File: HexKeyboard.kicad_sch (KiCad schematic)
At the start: 62 parts, among them J1 Conn_02x04_Odd_Even, J4 USB_A, J9 Micro_SD_Card, SW1 SW_3, SW10 SW_9, SW11 SW_8, SW12 SW_7, SW13 SW_Hash, SW14 SW_Hash, SW15 SW_0, SW16 SW_Star, SW17 SW_Hash, SW18 SW_Hash, SW19 SW_0, SW2 SW_3, SW20 SW_Star, SW3 SW_2, SW4 SW_1, SW5 SW_6, SW6 SW_6, SW7 SW_5, SW8 SW_4, SW9 SW_9, U1 ATmega32U4-AU, U2 AMS1117-3.3, U3 74LVC125, U4 AT24CS64-XHM, Y1 16MHz

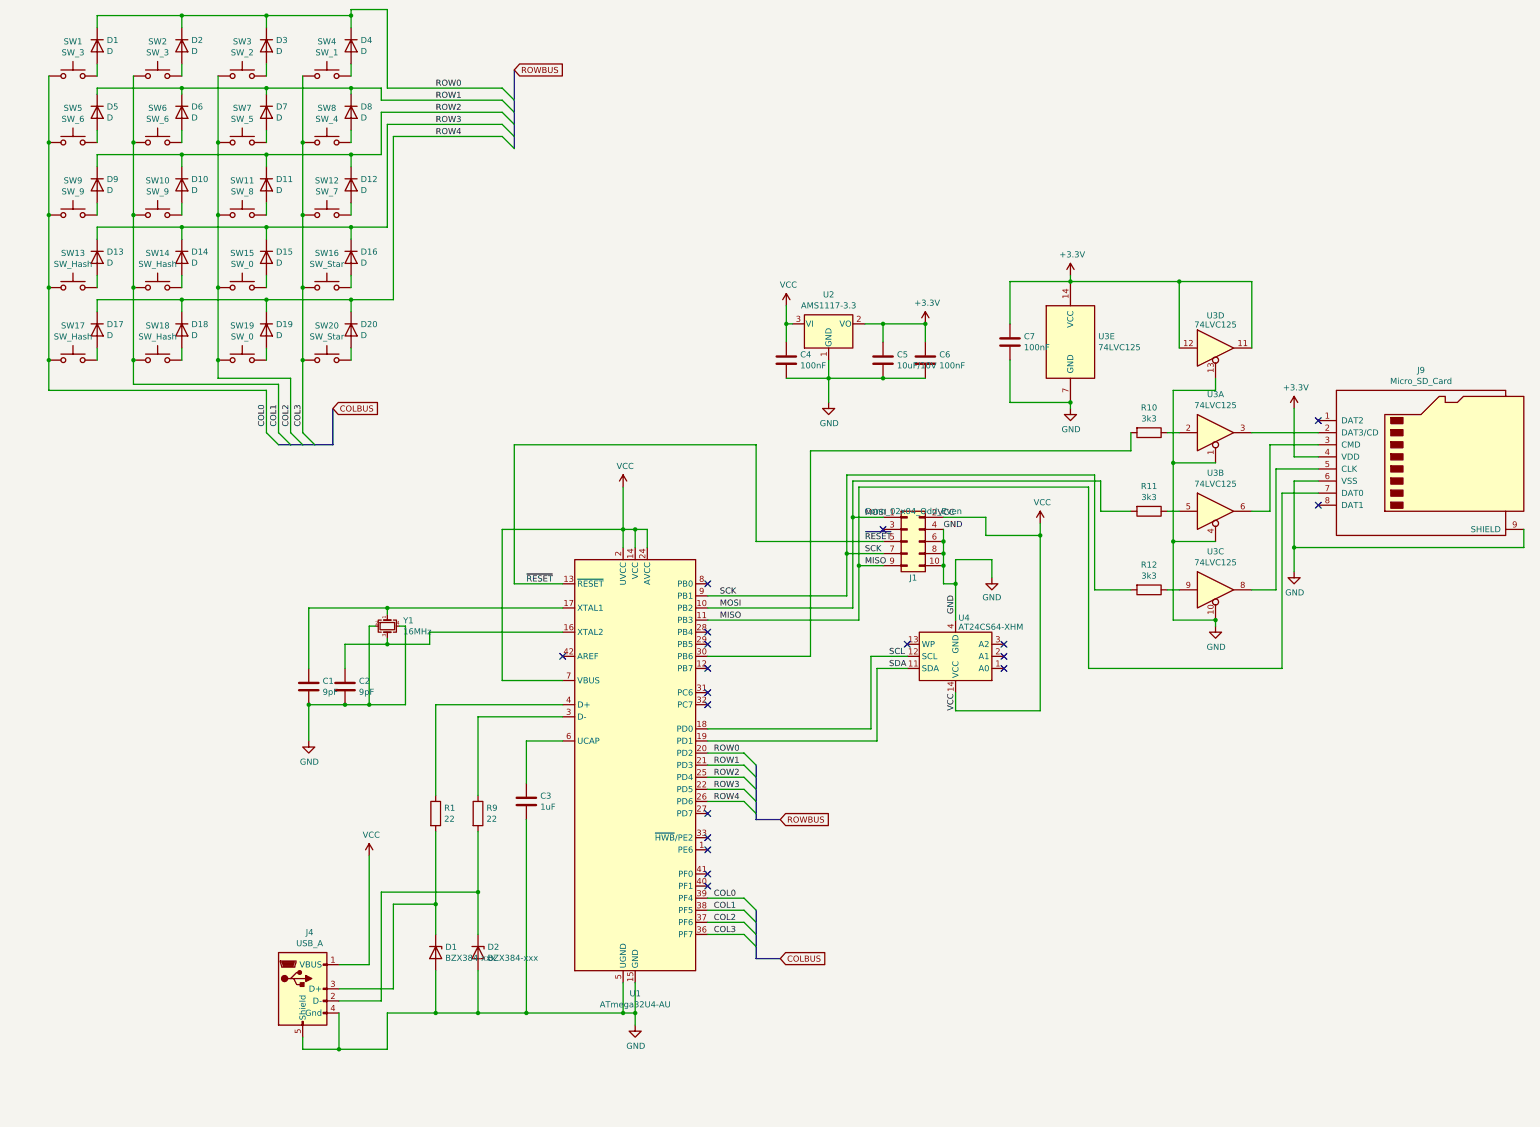
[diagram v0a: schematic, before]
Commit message: Cleaned up libraries Added Display Switched to USB-C
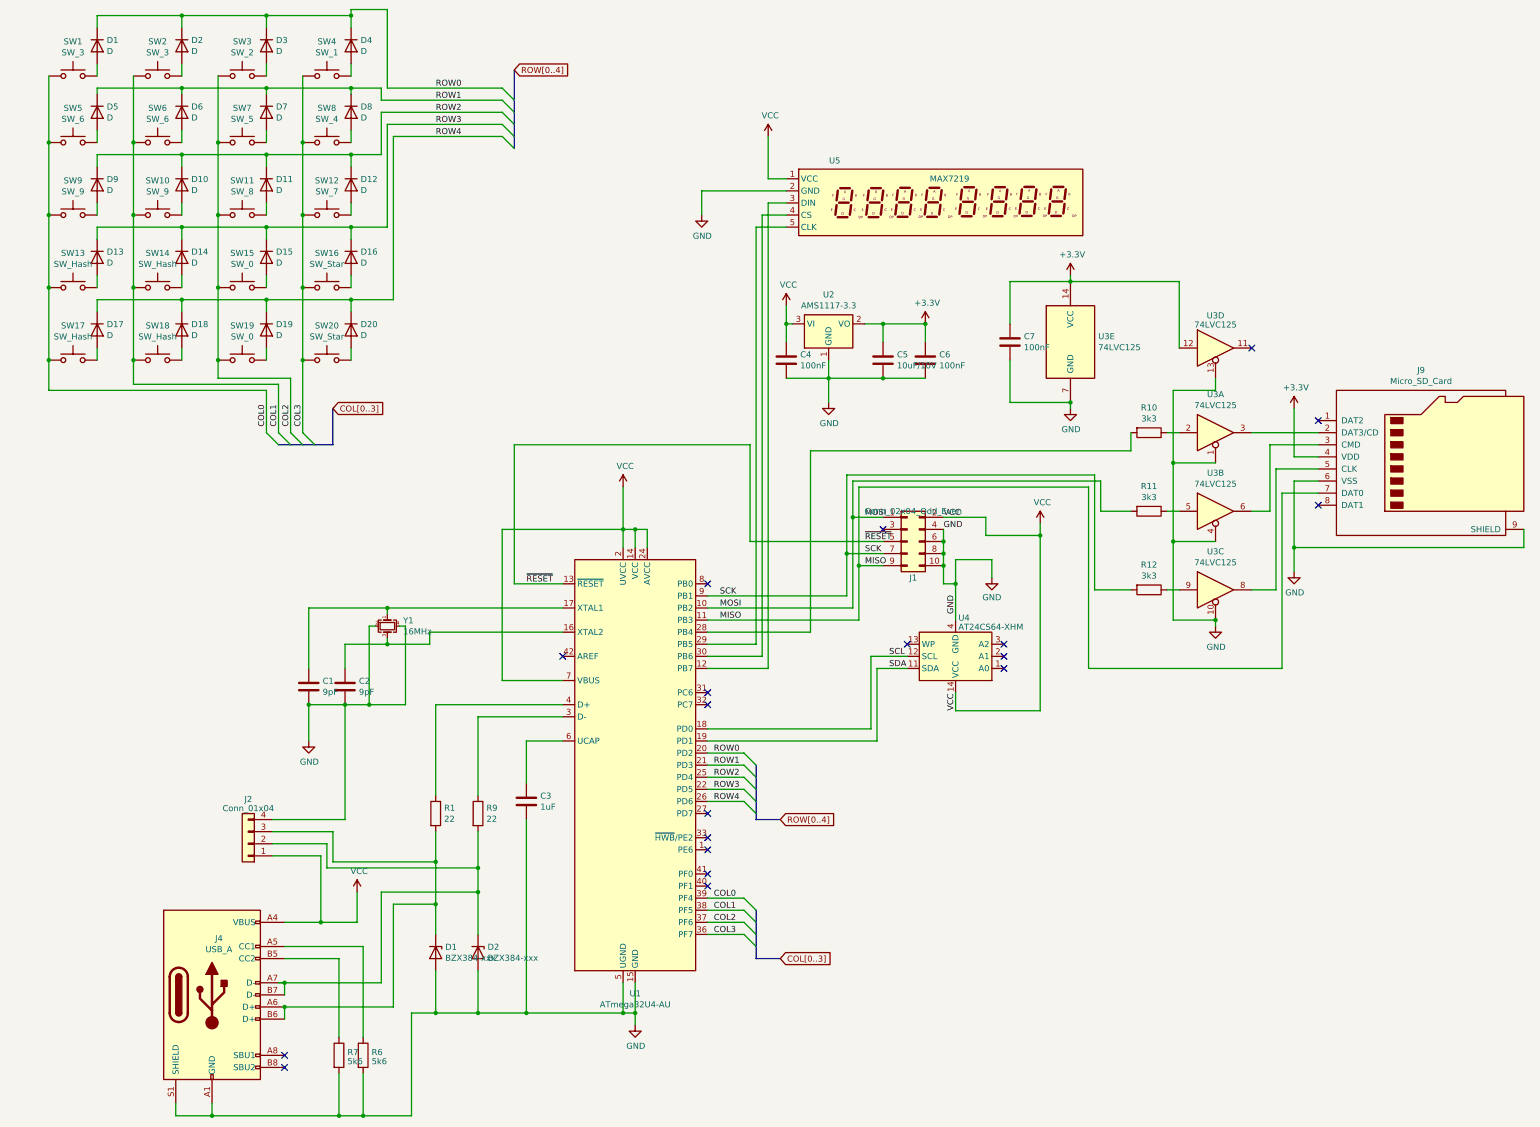
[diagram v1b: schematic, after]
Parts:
- added J2: Conn_01x04, Connector_PinHeader_2.54mm:PinHeader_1x04_P2.54mm_Vertical, symbol Connector_Generic:Conn_01x04
- added R6, R7: 5k6, Resistor_SMD:R_0603_1608Metric, symbol Device:R
- added U5: MAX7219, MyFootprints:Display_x8_MAX7219, symbol MySymbols:Display_x8_MAX7219
- C1, C2, C3, C4, C6, C7: footprint Capacitors_SMD:C_0603 -> Capacitor_SMD:C_0603_1608Metric
- C5: footprint Capacitors_SMD:C_0805 -> Capacitor_SMD:C_0805_2012Metric
- D1, D10, D11, D12, D13, D14, D15, D16, D17, D18, D19, D2, D20, D3, D4, D5, D6, D7, D8, D9: footprint Diodes_SMD:D_0603 -> Diode_SMD:D_0603_1608Metric
- D1, D2: footprint Diodes_SMD:D_SOD-323 -> Diode_SMD:D_SOD-323; symbol MuchPWM3-rescue:BZX384-xxx-Diode -> MySymbols:BZX384-xxx-Diode
- J4: footprint Connector_USB:USB_A_CNCTech_1001-011-01101_Horizontal -> Connector_USB:USB_C_Receptacle_G-Switch_GT-USB-7010ASV; symbol Connector:USB_B_Micro -> Connector:USB_C_Receptacle_USB2.0
- J9: footprint Connectors_Card:MicroSd_Wurth_693072010801 -> Connector_Card:microSD_HC_Wuerth_693072010801
- R1, R10, R11, R12, R9: footprint Resistors_SMD:R_0603 -> Resistor_SMD:R_0603_1608Metric
- U1: footprint Housings_QFP:LQFP-44_10x10mm_Pitch0.8mm -> Package_QFP:TQFP-44_10x10mm_P0.8mm; symbol MuchPWM3-rescue:ATmega32U4-AU-MCU_Microchip_ATmega -> MySymbols:ATmega32U4-AU-MCU_Microchip_ATmega
- U2: footprint TO_SOT_Packages_SMD:SOT-223-3_TabPin2 -> Package_TO_SOT_SMD:SOT-223-3_TabPin2
- U4: symbol ZIF:AT24CS64-XHM_in_ZIF14 -> MySymbols:AT24CS64-XHM_in_ZIF14
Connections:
- net +3.3V: no longer U3.11
- net GND: now also J4.A1 (GND), J4.A12 (GND), J4.B1 (GND), J4.B12 (GND), J4.S1 (SHIELD), J2.4 (Pin_4), R6.2, R7.2, U5.2 (GND); no longer J4.4 (Gnd), J4.5 (Shield)
- net VCC: now also J4.A4 (VBUS), J4.A9 (VBUS), J4.B4 (VBUS), J4.B9 (VBUS), J2.1 (Pin_1), U5.1 (VCC); no longer J4.1 (VBUS)
- net at D2.1 (K), R9.2: now also J4.A7 (D-), J4.B7 (D-), J2.2 (Pin_2); no longer J4.2 (D-)
- net at D1.1 (K), R1.2: now also J4.A6 (D+), J4.B6 (D+), J2.3 (Pin_3); no longer J4.3 (D+)
- net at U1.30 (PB6): now also U5.4 (CS); no longer R10.2
- net at U1.12 (PB7): now also U5.3 (DIN)
- net at U1.28 (PB4): now also R10.2
- net at U1.29 (PB5): now also U5.5 (CLK)
- new net: J4.A5 (CC1), R6.1
- new net: J4.B5 (CC2), R7.1

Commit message: Filled up matrix to 5x5 Started on layout
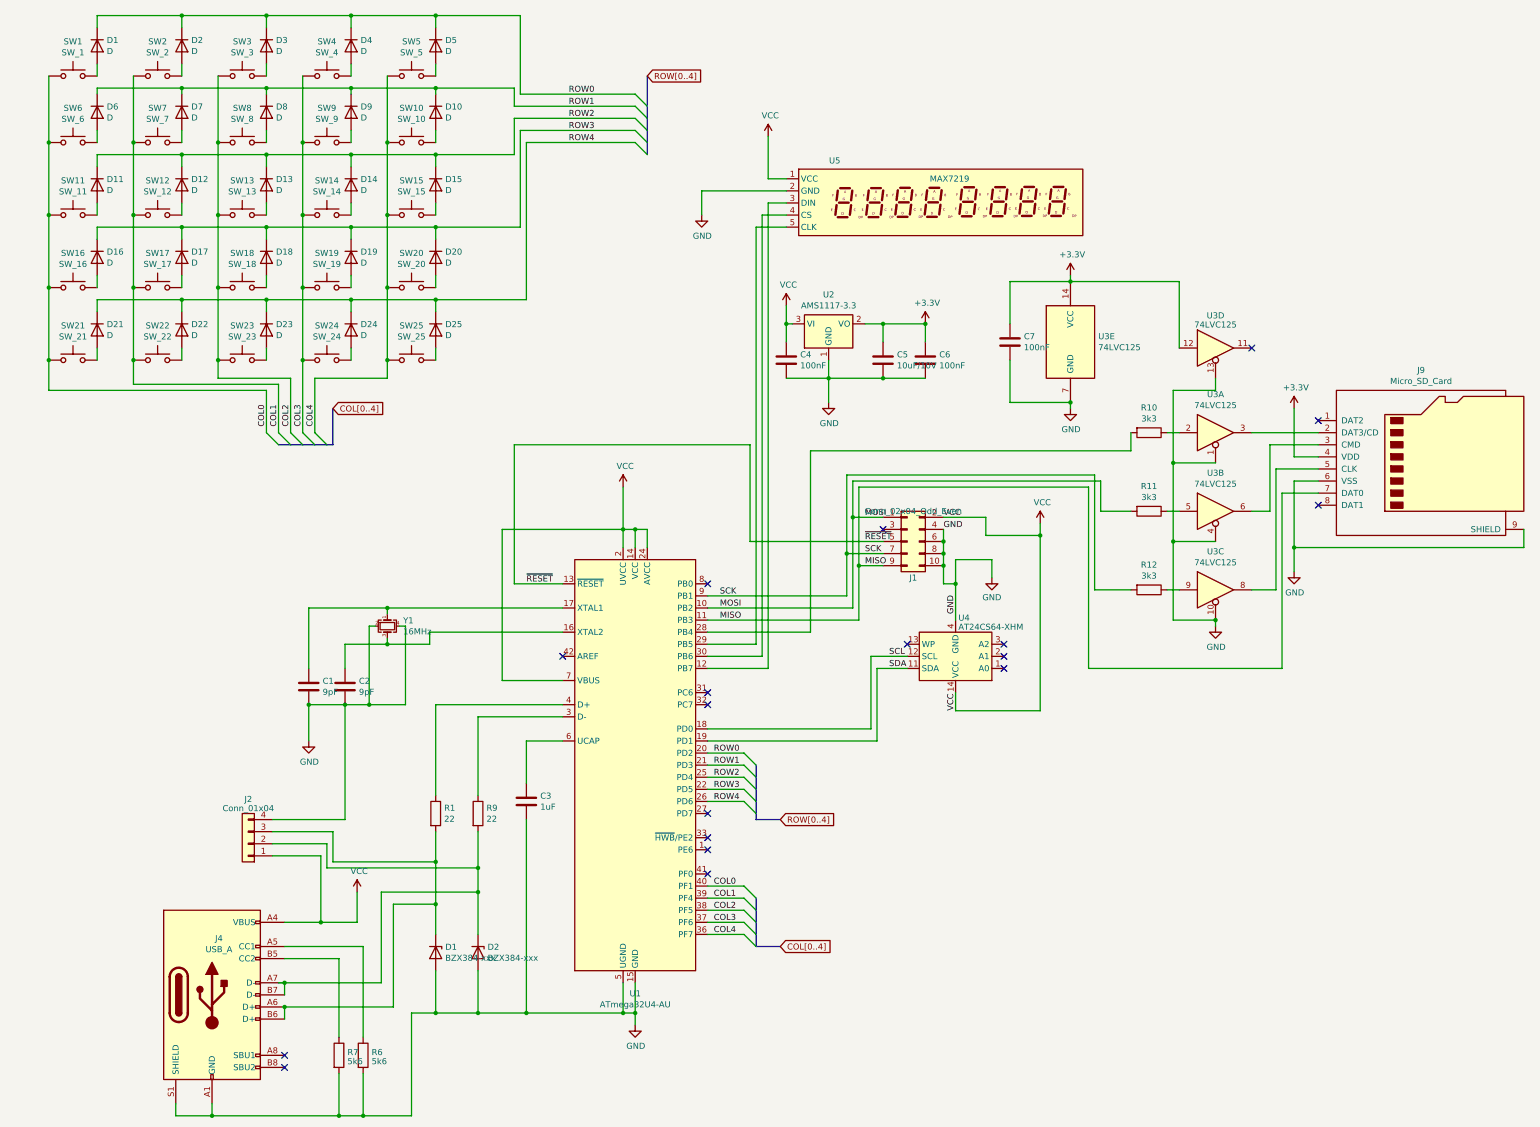
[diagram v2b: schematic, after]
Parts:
- added D10, D15, D20, D25, D5: D, Diode_SMD:D_0603_1608Metric, symbol Device:D
- added SW10: SW_10, keyswitches:Kailh_socket_MX_optional_compatible, symbol Switch:SW_Push
- added SW15: SW_15, keyswitches:Kailh_socket_MX_optional_compatible, symbol Switch:SW_Push
- added SW20: SW_20, keyswitches:Kailh_socket_MX_optional_compatible, symbol Switch:SW_Push
- added SW25: SW_25, keyswitches:Kailh_socket_MX_optional_compatible, symbol Switch:SW_Push
- added SW5: SW_5, keyswitches:Kailh_socket_MX_optional_compatible, symbol Switch:SW_Push
- SW1: value SW_3 -> SW_1
- SW11: renamed from SW9; value SW_9 -> SW_11
- SW12: renamed from SW10; value SW_9 -> SW_12
- SW13: renamed from SW11; value SW_8 -> SW_13
- SW14: renamed from SW12; value SW_7 -> SW_14
- SW16: renamed from SW13; value SW_Hash -> SW_16
- SW17: renamed from SW14; value SW_Hash -> SW_17
- SW18: renamed from SW15; value SW_0 -> SW_18
- SW19: renamed from SW16; value SW_Star -> SW_19
- SW2: value SW_3 -> SW_2
- SW21: renamed from SW17; value SW_Hash -> SW_21
- SW22: renamed from SW18; value SW_Hash -> SW_22
- SW23: renamed from SW19; value SW_0 -> SW_23
- SW24: renamed from SW20; value SW_Star -> SW_24
- SW3: value SW_2 -> SW_3
- SW4: value SW_1 -> SW_4
- SW7: renamed from SW6; value SW_6 -> SW_7
- SW8: renamed from SW7; value SW_5 -> SW_8
- SW9: renamed from SW8; value SW_4 -> SW_9
- renumbered D9 to D11, D10 to D12, D11 to D13, D12 to D14, D13 to D16, D14 to D17, D15 to D18, D16 to D19, D17 to D21, D18 to D22, D19 to D23, D20 to D24, D5 to D6, D6 to D7, D7 to D8, D8 to D9, SW5 to SW6
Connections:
- net COL0: now also U1.40 (PF1); no longer U1.39 (PF4)
- net COL1: now also U1.39 (PF4); no longer U1.38 (PF5)
- net COL2: now also U1.38 (PF5); no longer U1.37 (PF6)
- net COL3: now also U1.37 (PF6); no longer U1.36 (PF7)
- net ROW0: now also D5.1 (K)
- net ROW1: now also D10.1 (K)
- net ROW2: now also D15.1 (K)
- net ROW3: now also D20.1 (K)
- net ROW4: now also D25.1 (K)
- new net: D20.2 (A), SW20.2
- new net: D25.2 (A), SW25.2
- new net: D5.2 (A), SW5.2
- new net: D15.2 (A), SW15.2
- new net: D10.2 (A), SW10.2
- new net COL4: SW10.1, SW15.1, SW20.1, SW25.1, SW5.1, U1.36 (PF7)
- no-connect marks 19 -> 18

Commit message: Finished layout and routing
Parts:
- added H1, H2, H3, H4, H5, H6: MountingHole_Pad, MountingHole:MountingHole_3.2mm_M3_Pad_Via, symbol Mechanical:MountingHole_Pad
- J4: LCSC C2681564 -> C2988369
- J9: LCSC C86574 -> C5912397
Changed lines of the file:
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@@
       (effects (font (size 1.27 1.27)) hide)
     )
-    (property "LCSC" "C2681564" (at 85.09 245.11 0)
+    (property "LCSC" "C2988369" (at 85.09 245.11 0)
       (effects (font (size 1.27 1.27)) hide)
     )
@@
       (effects (font (size 1.27 1.27)) hide)
     )
-    (property "LCSC" "C86574" (at 340.36 132.08 0)
+    (property "LCSC" "C5912397" (at 340.36 132.08 0)
       (effects (font (size 1.27 1.27)) hide)
     )
@@
         (path "/cd9850cf-ce78-4253-97c8-d3ca58ada4b0"
           (reference "SW22") (unit 1)
+        )
+      )
+    )
+  )
+  (symbol (lib_id "Mechanical:MountingHole_Pad") (at 46.99 198.12 0) (unit 1)
+    (in_bom yes) (on_board yes) (dnp no) (fields_autoplaced)
+    (property "Reference" "H4" (at 49.53 196.2063 0)
+      (effects (font (size 1.27 1.27)) (justify left))
+    )
+    (property "Value" "MountingHole_Pad" (at 49.53 198.1273 0)
+      (effects (font (size 1.27 1.27)) (justify left))
+    )
+    (property "Footprint" "MountingHole:MountingHole_3.2mm_M3_Pad_Via" (at 46.99 198.12 0)
+      (effects (font (size 1.27 1.27)) hide)
+    )
+    (property "Datasheet" "~" (at 46.99 198.12 0)
+      (effects (font (size 1.27 1.27)) hide)
+    )
+    (pin "1")
+    (instances
+      (project "HexKeyboard"
+        (path "/cd9850cf-ce78-4253-97c8-d3ca58ada4b0"
+          (reference "H4") (unit 1)
         )
       )
@@
     )
   )
+  (symbol (lib_id "Mechanical:MountingHole_Pad") (at 48.26 210.82 0) (unit 1)
+    (in_bom yes) (on_board yes) (dnp no) (fields_autoplaced)
+    (property "Reference" "H5" (at 50.8 208.9063 0)
+      (effects (font (size 1.27 1.27)) (justify left))
+    )
+    (property "Value" "MountingHole_Pad" (at 50.8 210.8273 0)
+      (effects (font (size 1.27 1.27)) (justify left))
+    )
+    (property "Footprint" "MountingHole:MountingHole_3.2mm_M3_Pad_Via" (at 48.26 210.82 0)
+      (effects (font (size 1.27 1.27)) hide)
+    )
+    (property "Datasheet" "~" (at 48.26 210.82 0)
+      (effects (font (size 1.27 1.27)) hide)
+    )
+    (pin "1")
+    (instances
+      (project "HexKeyboard"
+        (path "/cd9850cf-ce78-4253-97c8-d3ca58ada4b0"
+          (reference "H5") (unit 1)
+        )
+      )
+    )
+  )
   (symbol (lib_id "power:GND") (at 248.92 157.48 0) (unit 1)
     (in_bom yes) (on_board yes) (dnp no) (fields_autoplaced)
@@
         (path "/cd9850cf-ce78-4253-97c8-d3ca58ada4b0"
           (reference "C4") (unit 1)
+        )
+      )
+    )
+  )
+  (symbol (lib_id "Mechanical:MountingHole_Pad") (at 44.45 229.87 0) (unit 1)
+    (in_bom yes) (on_board yes) (dnp no) (fields_autoplaced)
+    (property "Reference" "H6" (at 46.99 227.9563 0)
+      (effects (font (size 1.27 1.27)) (justify left))
+    )
+    (property "Value" "MountingHole_Pad" (at 46.99 229.8773 0)
+      (effects (font (size 1.27 1.27)) (justify left))
+    )
+    (property "Footprint" "MountingHole:MountingHole_3.2mm_M3_Pad_Via" (at 44.45 229.87 0)
+      (effects (font (size 1.27 1.27)) hide)
+    )
+    (property "Datasheet" "~" (at 44.45 229.87 0)
+      (effects (font (size 1.27 1.27)) hide)
+    )
+    (pin "1")
+    (instances
+      (project "HexKeyboard"
+        (path "/cd9850cf-ce78-4253-97c8-d3ca58ada4b0"
+          (reference "H6") (unit 1)
         )
       )
@@
     )
   )
+  (symbol (lib_id "Mechanical:MountingHole_Pad") (at 48.26 161.29 0) (unit 1)
+    (in_bom yes) (on_board yes) (dnp no) (fields_autoplaced)
+    (property "Reference" "H2" (at 50.8 159.3763 0)
+      (effects (font (size 1.27 1.27)) (justify left))
+    )
+    (property "Value" "MountingHole_Pad" (at 50.8 161.2973 0)
+      (effects (font (size 1.27 1.27)) (justify left))
+    )
+    (property "Footprint" "MountingHole:MountingHole_3.2mm_M3_Pad_Via" (at 48.26 161.29 0)
+      (effects (font (size 1.27 1.27)) hide)
+    )
+    (property "Datasheet" "~" (at 48.26 161.29 0)
+      (effects (font (size 1.27 1.27)) hide)
+    )
+    (pin "1")
+    (instances
+      (project "HexKeyboard"
+        (path "/cd9850cf-ce78-4253-97c8-d3ca58ada4b0"
+          (reference "H2") (unit 1)
+        )
+      )
+    )
+  )
   (symbol (lib_id "74xx:74LS125") (at 295.91 109.22 0) (unit 4)
     (in_bom yes) (on_board yes) (dnp no) (fields_autoplaced)
@@
     )
   )
+  (symbol (lib_id "Mechanical:MountingHole_Pad") (at 45.72 179.07 0) (unit 1)
+    (in_bom yes) (on_board yes) (dnp no) (fields_autoplaced)
+    (property "Reference" "H3" (at 48.26 177.1563 0)
+      (effects (font (size 1.27 1.27)) (justify left))
+    )
+    (property "Value" "MountingHole_Pad" (at 48.26 179.0773 0)
+      (effects (font (size 1.27 1.27)) (justify left))
+    )
+    (property "Footprint" "MountingHole:MountingHole_3.2mm_M3_Pad_Via" (at 45.72 179.07 0)
+      (effects (font (size 1.27 1.27)) hide)
+    )
+    (property "Datasheet" "~" (at 45.72 179.07 0)
+      (effects (font (size 1.27 1.27)) hide)
+    )
+    (pin "1")
+    (instances
+      (project "HexKeyboard"
+        (path "/cd9850cf-ce78-4253-97c8-d3ca58ada4b0"
+          (reference "H3") (unit 1)
+        )
+      )
+    )
+  )
   (symbol (lib_id "power:VCC") (at 115.57 223.52 0) (unit 1)
     (in_bom yes) (on_board yes) (dnp no)
@@
         )
       )
+    )
+  )
+  (symbol (lib_id "Mechanical:MountingHole_Pad") (at 48.26 146.05 0) (unit 1)
+    (in_bom yes) (on_board yes) (dnp no) (fields_autoplaced)
+    (property "Reference" "H1" (at 50.8 144.1363 0)
+      (effects (font (size 1.27 1.27)) (justify left))
+    )
+    (property "Value" "MountingHole_Pad" (at 50.8 146.0573 0)
+      (effects (font (size 1.27 1.27)) (justify left))
+    )
+    (property "Footprint" "MountingHole:MountingHole_3.2mm_M3_Pad_Via" (at 48.26 146.05 0)
+      (effects (font (size 1.27 1.27)) hide)
+    )
+    (property "Datasheet" "~" (at 48.26 146.05 0)
+      (effects (font (size 1.27 1.27)) hide)
+    )
+    (pin "1")
+    (instances
+      (project "HexKeyboard"
+        (path "/cd9850cf-ce78-4253-97c8-d3ca58ada4b0"
+          (reference "H1") (unit 1)
+        )
+      )
